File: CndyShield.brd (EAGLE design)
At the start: 69.9 x 78.1 mm, 20 parts, among them U1 ARDUINOR3-BPLACE

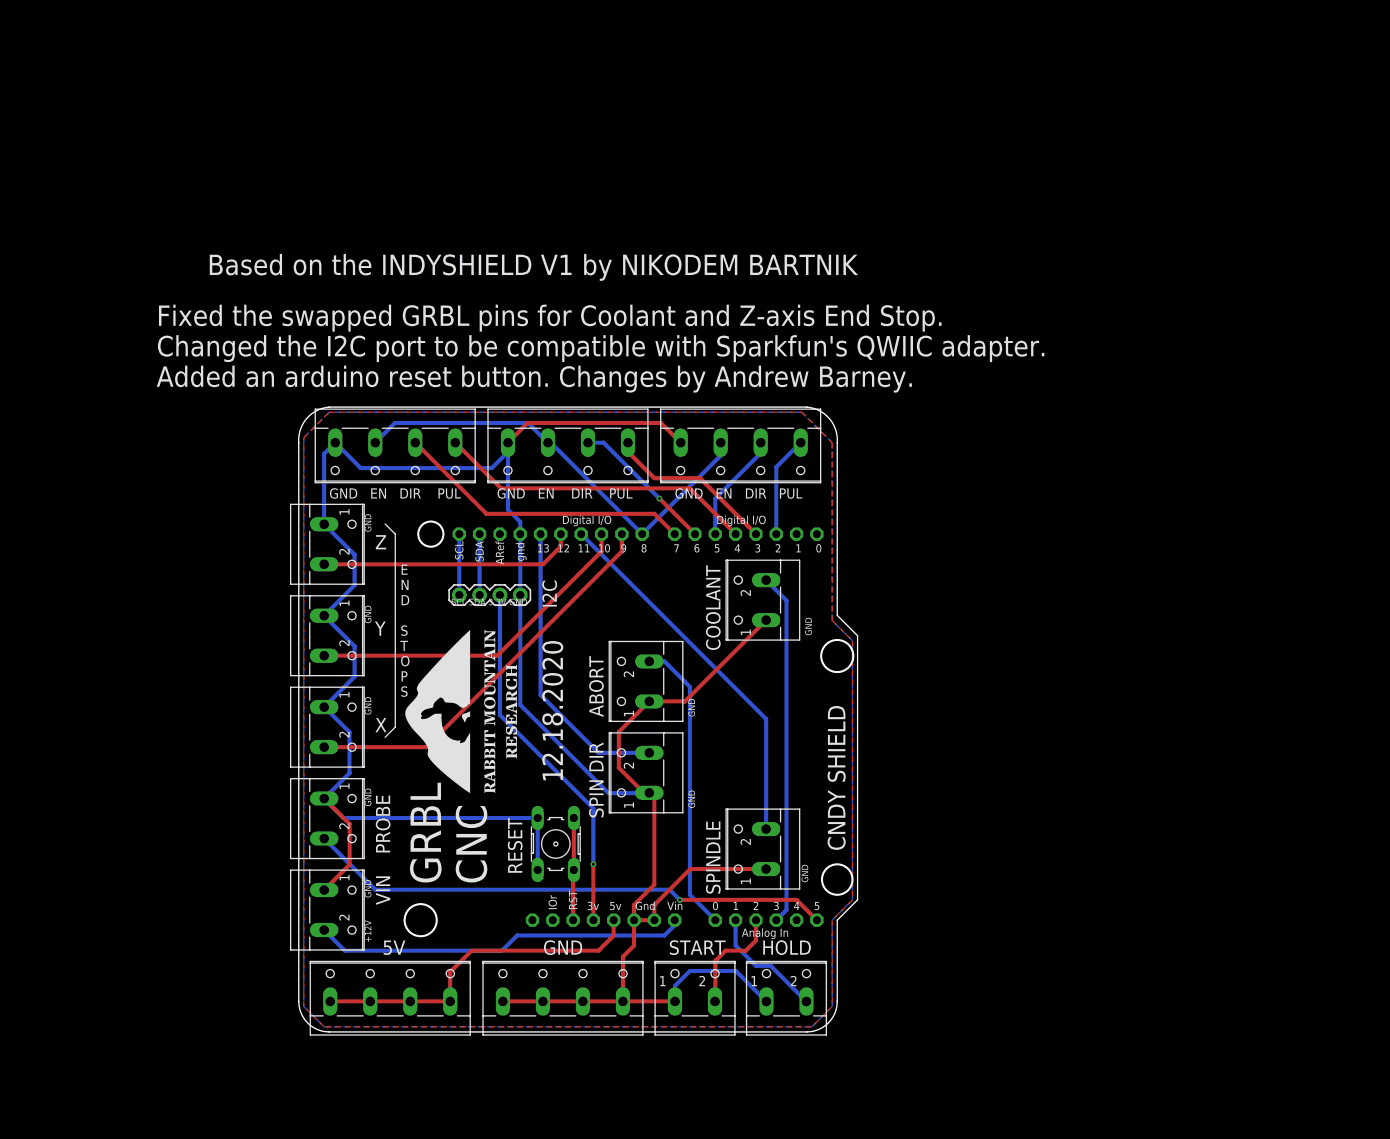
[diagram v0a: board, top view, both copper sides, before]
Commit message: Add files via upload
V1.1 : remapped analog breakouts. Added filter capacitors. Added Alarm State LED on A4.
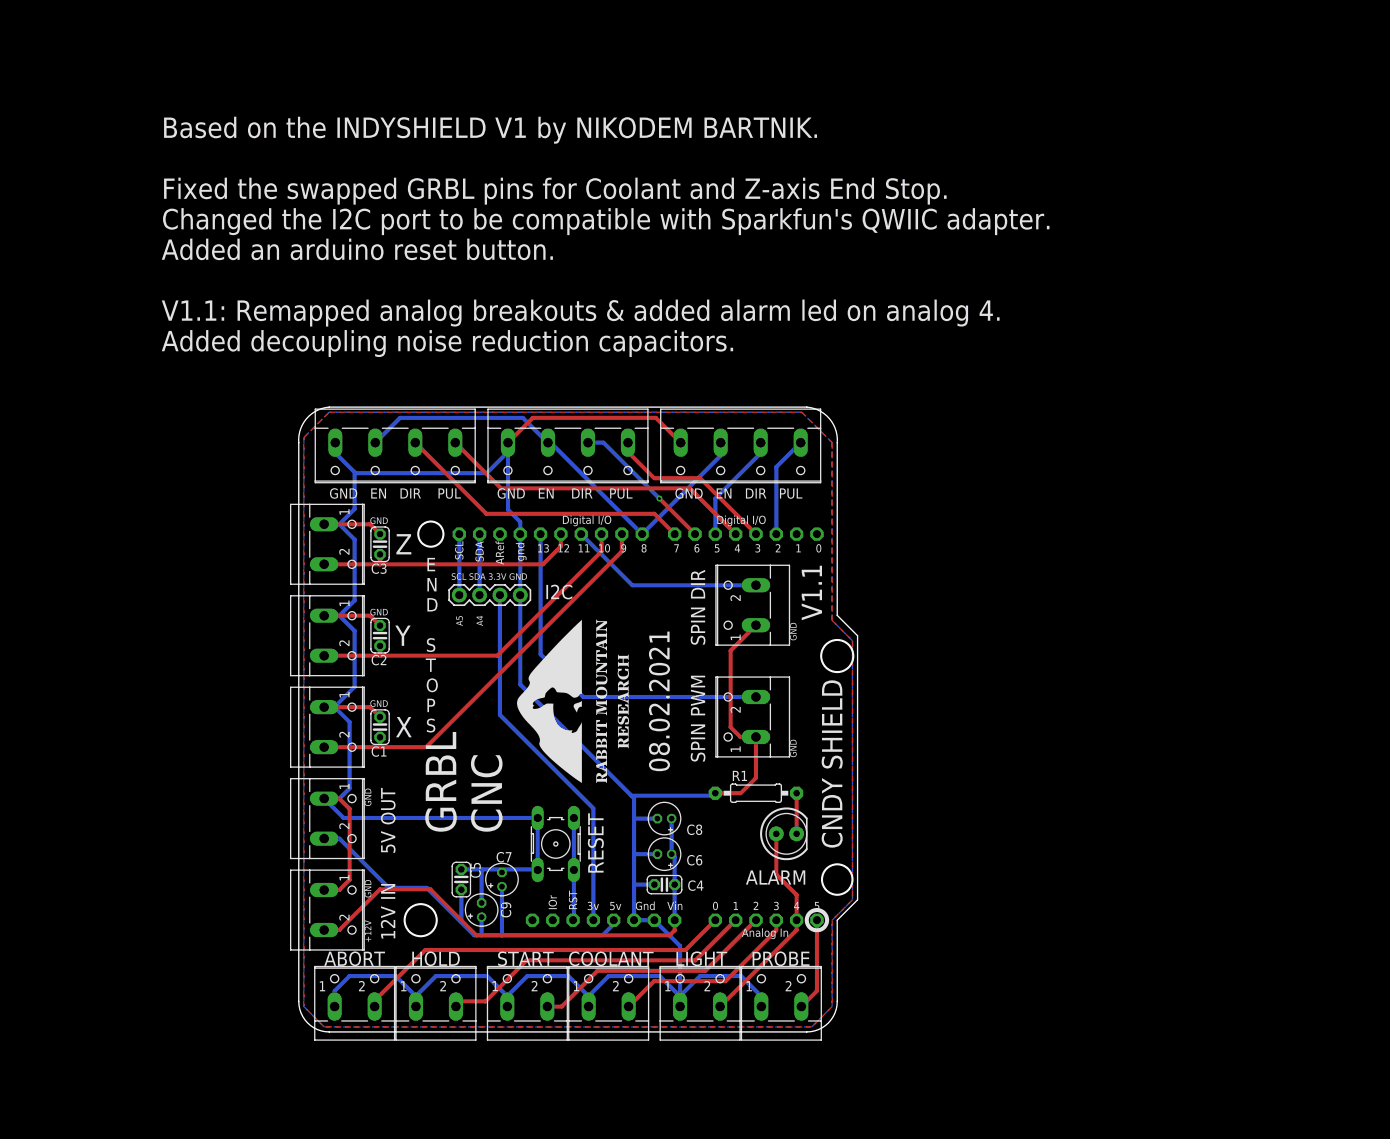
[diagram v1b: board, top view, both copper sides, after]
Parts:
- removed GND: (no value), con-wago-500:W237-4
- removed RESET: (no value), con-wago-500:W237-102
- added ABORT, LIGHT: (no value), con-wago-500:W237-102
- added C1, C2, C3, C4, C5: (no value), adafruit:C025-024X044
- added C6, C7, C8, C9: (no value), adafruit:E1,8-4
- added D1: (no value), SparkFun-LED:LED_5MM
- added R1: 330, adafruit:0207/10
- 5V: device con-wago-500:W237-4 -> con-wago-500:W237-102
- moved PROBE 60.1 mm to (95.9, 15.9), turned to 0 degrees
- moved COOL 52.8 mm to (74.3, 15.9), turned to 0 degrees
- moved HOLD 43.8 mm to (52.7, 15.9)
- moved SPIN_E 30.5 mm to (91.4, 64.8)
- moved 5V 22.7 mm to (40.0, 38.1), turned to 270 degrees
- moved START 21.0 mm to (64.1, 15.9)
- moved SPIN_DIR 15.1 mm to (91.4, 50.8)
- moved U$2 14.0 mm to (76.8, 42.5)
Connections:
- removed net RESET: RESET.2, U1.A0
- new net ABORT: ABORT.2, U1.A0
- new net LIGHT: D1.A, LIGHT.2, U1.A4
- new net N$8: D1.K, R1.2
- net +12V: now also C4.1, C6.+, C8.+
- net +5V: now also C5.1, C7.+, C9.+; no longer 5V.1, 5V.3, 5V.4
- net GND: now also 5V.1, ABORT.1, C1.2, C2.2, C3.2, C4.2, C5.2, C6.-, C7.-, C8.-, C9.-, LIGHT.1, R1.1; no longer GND.1, GND.2, GND.3, GND.4, RESET.1
- net LIM_X: now also C1.1
- net LIM_Y: now also C2.1
- net LIM_Z: now also C3.1
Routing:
- net GND: track 324.3 -> 396.5 mm
- net PROBE: track 65.8 -> 11.6 mm, vias 1 -> 0
- net ABORT: track 0.00 -> 47.5 mm
- net RESET: track 36.9 -> 0.00 mm
- net LIGHT: track 0.00 -> 26.6 mm
- net HOLD: track 14.9 -> 39.8 mm
- net SPIN_E: track 46.4 -> 24.5 mm
- net COOL: track 44.1 -> 23.7 mm
- net START: track 13.8 -> 30.5 mm
- net +12V: track 46.8 -> 62.7 mm
- net +5V: track 42.9 -> 54.7 mm
- net SPIN_DIR: track 36.7 -> 44.2 mm
- net N$8: track 0.00 -> 5.08 mm
- net LIM_Z: track 32.0 -> 33.3 mm
- net LIM_Y: track 42.2 -> 43.5 mm
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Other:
- board text added: "08.02.2021"
- board text added: "12V IN"
- board text added: "5V OUT"
- board text added: "A4"
- board text added: "A5"
- board text added: "ALARM"
- board text added: "Based on the INDYSHIELD V1 by NIKODEM BARTNIK. Fixed the swapped GRBL pins for Coolant and Z-axis End Stop. Changed the I2C port to be compatible with Sparkfun's QWIIC adapter. Added an arduino reset button. V1.1: Remapped analog breakouts & added alarm led on analog 4. Added decoupling noise reduction capacitors."
- board text added: "LIGHT"
- board text added: "SPIN PWM"
- board text added: "V1.1"
- board text removed: "12.18.2020"
- board text removed: "5V"
- board text removed: "Based on the INDYSHIELD V1 by NIKODEM BARTNIK"
- board text removed: "Fixed the swapped GRBL pins for Coolant and Z-axis End Stop. Changed the I2C port to be compatible with Sparkfun's QWIIC adapter. Added an arduino reset button. Changes by Andrew Barney."
- board text removed: "SPINDLE"
- board text removed: "VIN"

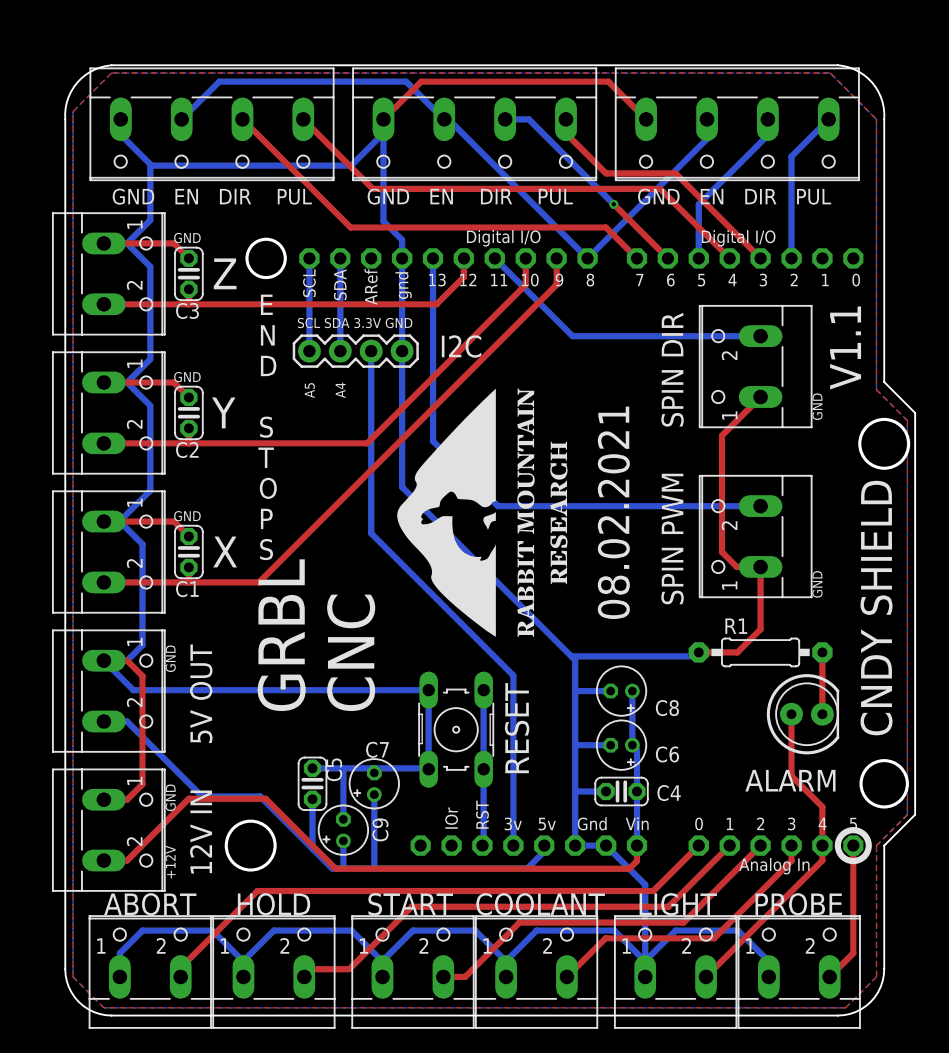
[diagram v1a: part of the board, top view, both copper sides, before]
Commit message: Add files via upload
minor silkscreen change for Analog 4. Changed LIGHT to MIST to be more consistent with official GRBL port use.
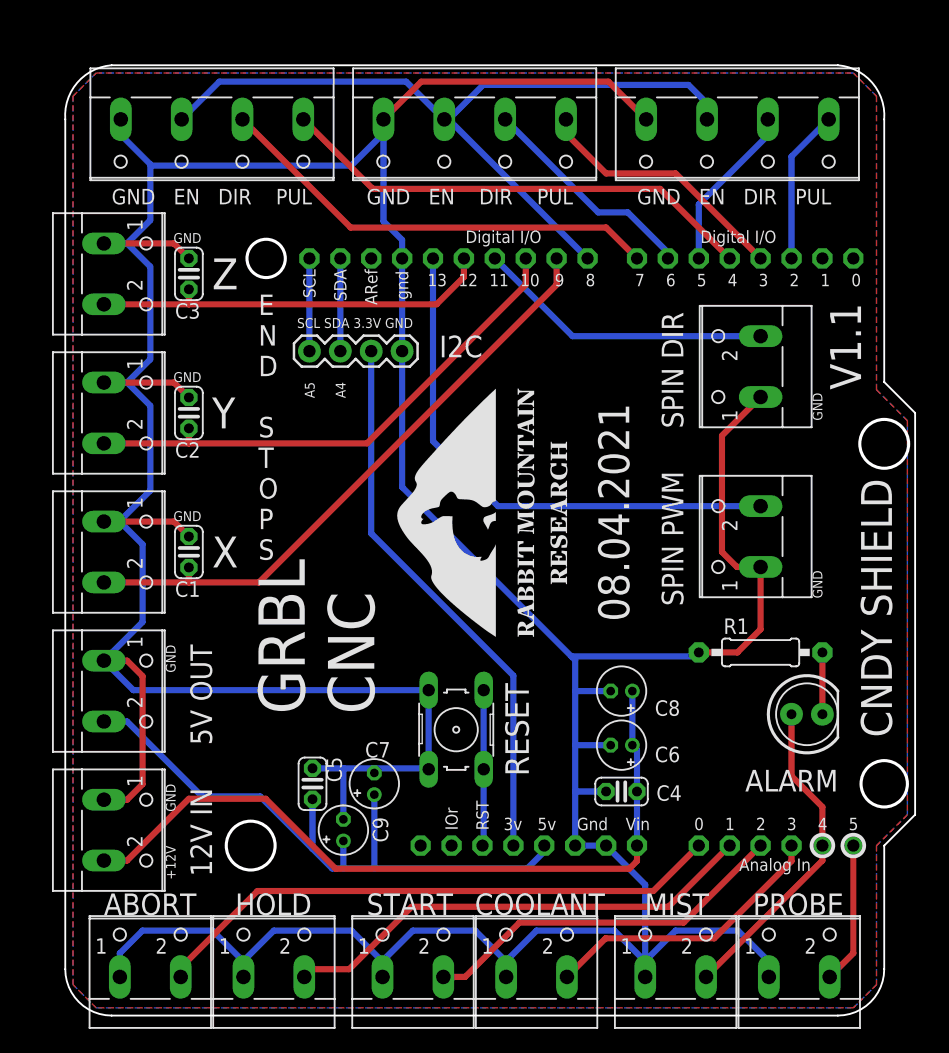
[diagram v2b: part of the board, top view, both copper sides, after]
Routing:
- net S_EN: track 56.2 -> 65.4 mm
- net GND: track 396.5 -> 395.3 mm
- net N$3: track 18.1 -> 18.4 mm, vias 1 -> 0
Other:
- board text added: "08.04.2021"
- board text added: "MIST"
- board text removed: "08.02.2021"
- board text removed: "LIGHT"
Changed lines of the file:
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@@
 V1.1: Remapped analog breakouts &amp; added alarm led on analog 4.
 Added decoupling noise reduction capacitors.</text>
-<text x="81.915" y="43.815" size="2.54" layer="25" rot="R90">08.02.2021</text>
+<text x="81.915" y="43.815" size="2.54" layer="25" rot="R90">08.04.2021</text>
 <text x="97.79" y="45.72" size="0.8128" layer="25" rot="R90">GND</text>
 <text x="97.79" y="60.325" size="0.8128" layer="25" rot="R90">GND</text>
@@
 <text x="49.53" y="19.685" size="1.778" layer="21" font="vector" ratio="20">HOLD</text>
 <text x="60.325" y="19.685" size="1.778" layer="21" font="vector" ratio="20">START</text>
-<text x="82.55" y="19.685" size="1.778" layer="21" font="vector" ratio="20">LIGHT</text>
+<text x="83.185" y="19.685" size="1.778" layer="21" font="vector" ratio="20">MIST</text>
 <text x="92.075" y="19.685" size="1.778" layer="21" font="vector" ratio="20">PROBE</text>
 <text x="100.965" y="62.865" size="2.54" layer="21" font="vector" ratio="20" rot="R90">V1.1</text>
 <text x="47.625" y="22.86" size="1.778" layer="21" font="vector" ratio="20" rot="R90">12V IN</text>
 <text x="47.625" y="33.655" size="1.778" layer="21" font="vector" ratio="20" rot="R90">5V OUT</text>
-<circle x="100.33" y="25.4" radius="1.27" width="0.508" layer="21"/>
 <text x="91.44" y="29.845" size="1.778" layer="21" font="vector" ratio="20">ALARM</text>
 <text x="55.245" y="63.5" size="0.8128" layer="25" rot="R270">A5</text>
@@
 <text x="47.625" y="59.69" size="2.54" layer="21" font="vector" ratio="20">Y</text>
 <text x="47.625" y="71.12" size="2.54" layer="21" font="vector" ratio="20">Z</text>
+<circle x="100.33" y="25.4" radius="0.898025" width="0.3048" layer="21"/>
+<circle x="97.79" y="25.4" radius="0.898025" width="0.3048" layer="21"/>
 </plain>
 <attributes>
@@
 <wire x1="64.8138" y1="88.1888" x2="80.2062" y2="88.1888" width="0.508" layer="1"/>
 <polygon width="0.508" layer="1" spacing="0.8128" isolate="0.3048" orphans="yes">
-<vertex x="36.195" y="14.605"/>
-<vertex x="36.195" y="85.725"/>
-<vertex x="39.37" y="88.9"/>
-<vertex x="98.425" y="88.9"/>
-<vertex x="102.235" y="85.09"/>
+<vertex x="36.195" y="13.97"/>
+<vertex x="36.195" y="86.995"/>
+<vertex x="38.1" y="88.9"/>
+<vertex x="100.33" y="88.9"/>
+<vertex x="102.235" y="86.995"/>
 <vertex x="102.235" y="62.865"/>
 <vertex x="104.775" y="60.325"/>
 <vertex x="104.775" y="27.94"/>
 <vertex x="102.235" y="25.4"/>
-<vertex x="102.235" y="14.605"/>
-<vertex x="99.695" y="12.065"/>
-<vertex x="38.735" y="12.065"/>
+<vertex x="102.235" y="13.97"/>
+<vertex x="100.33" y="12.065"/>
+<vertex x="38.1" y="12.065"/>
 </polygon>
 <wire x1="38.735" y1="74.89" x2="40.64" y2="74.89" width="0.508" layer="16"/>
@@
 <wire x1="40.005" y1="52.03" x2="38.735" y2="52.03" width="0.508" layer="16"/>
 <wire x1="42.545" y1="61.555" x2="42.545" y2="54.57" width="0.508" layer="16"/>
-<wire x1="38.735" y1="40.6" x2="40.64" y2="40.6" width="0.508" layer="16"/>
-<wire x1="41.91" y1="41.87" x2="40.64" y2="40.6" width="0.508" layer="16"/>
+<wire x1="41.91" y1="43.775" x2="38.735" y2="40.6" width="0.508" layer="16"/>
 <wire x1="41.91" y1="50.165" x2="40.025" y2="52.05" width="0.508" layer="16"/>
-<wire x1="41.91" y1="41.87" x2="41.91" y2="50.165" width="0.508" layer="16"/>
+<wire x1="41.91" y1="43.775" x2="41.91" y2="50.165" width="0.508" layer="16"/>
 <contactref element="LY1" pad="1"/>
 <wire x1="41.91" y1="30.44" x2="40.64" y2="29.17" width="0.508" layer="1"/>
@@
 <contactref element="Z" pad="3"/>
 <contactref element="Y" pad="3"/>
-<wire x1="78.486" y1="73.66" x2="88.305" y2="83.479" width="0.508" layer="16"/>
-<wire x1="88.305" y1="83.479" x2="88.305" y2="85.09" width="0.508" layer="16"/>
 <wire x1="78.486" y1="73.66" x2="67.056" y2="85.09" width="0.508" layer="16"/>
 <wire x1="67.056" y1="85.09" x2="66.715" y2="85.09" width="0.508" layer="16"/>
@@
 <wire x1="48.2238" y1="88.1888" x2="63.5762" y2="88.1888" width="0.508" layer="16"/>
 <wire x1="63.5762" y1="88.1888" x2="66.675" y2="85.09" width="0.508" layer="16"/>
+<wire x1="67.07369375" y1="85.09" x2="66.715" y2="85.09" width="0.508" layer="16"/>
+<wire x1="69.90579375" y1="87.9221" x2="67.07369375" y2="85.09" width="0.508" layer="16"/>
+<wire x1="86.77920625" y1="87.9221" x2="69.90579375" y2="87.9221" width="0.508" layer="16"/>
+<wire x1="88.305" y1="85.09" x2="88.305" y2="86.39630625" width="0.508" layer="16"/>
+<wire x1="88.305" y1="86.39630625" x2="86.77920625" y2="87.9221" width="0.508" layer="16"/>
 </signal>
 <signal name="N$1">
@@
 <contactref element="U1" pad="D6"/>
 <contactref element="Y" pad="2"/>
-<wire x1="85.09" y1="73.66" x2="80.645" y2="78.105" width="0.508" layer="1"/>
-<via x="80.645" y="78.105" extent="1-16" drill="0.35"/>
-<wire x1="80.645" y1="78.105" x2="73.66" y2="85.09" width="0.508" layer="16"/>
-<wire x1="73.66" y1="85.09" x2="71.715" y2="85.09" width="0.508" layer="16"/>
+<wire x1="71.715" y1="85.09" x2="79.3604" y2="77.4446" width="0.508" layer="16"/>
+<wire x1="79.3604" y1="77.4446" x2="81.79553125" y2="77.4446" width="0.508" layer="16"/>
+<wire x1="85.09" y1="73.66" x2="85.09" y2="74.15013125" width="0.508" layer="16"/>
+<wire x1="85.09" y1="74.15013125" x2="81.79553125" y2="77.4446" width="0.508" layer="16"/>
 </signal>
 <signal name="N$4">
@@
 <signal name="VCC">
 <polygon width="0.508" layer="16" spacing="0.8128" isolate="0.3048" orphans="yes">
-<vertex x="36.195" y="85.725"/>
-<vertex x="36.195" y="14.605"/>
-<vertex x="38.735" y="12.065"/>
-<vertex x="99.695" y="12.065"/>
-<vertex x="102.235" y="14.605"/>
+<vertex x="36.195" y="86.995"/>
+<vertex x="36.195" y="13.97"/>
+<vertex x="38.1" y="12.065"/>
+<vertex x="100.33" y="12.065"/>
+<vertex x="102.235" y="13.97"/>
 <vertex x="102.235" y="25.4"/>
 <vertex x="104.775" y="27.94"/>
 <vertex x="104.775" y="60.325"/>
 <vertex x="102.235" y="62.865"/>
-<vertex x="102.235" y="85.09"/>
-<vertex x="98.425" y="88.9"/>
-<vertex x="39.37" y="88.9"/>
+<vertex x="102.235" y="86.995"/>
+<vertex x="100.33" y="88.9"/>
+<vertex x="38.1" y="88.9"/>
 </polygon>
 </signal>
